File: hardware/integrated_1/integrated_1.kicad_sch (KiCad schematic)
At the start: 6 parts, among them J1 USB4105-GF-A-120, J2 HDMI_A_1.4, J3 DEBUG

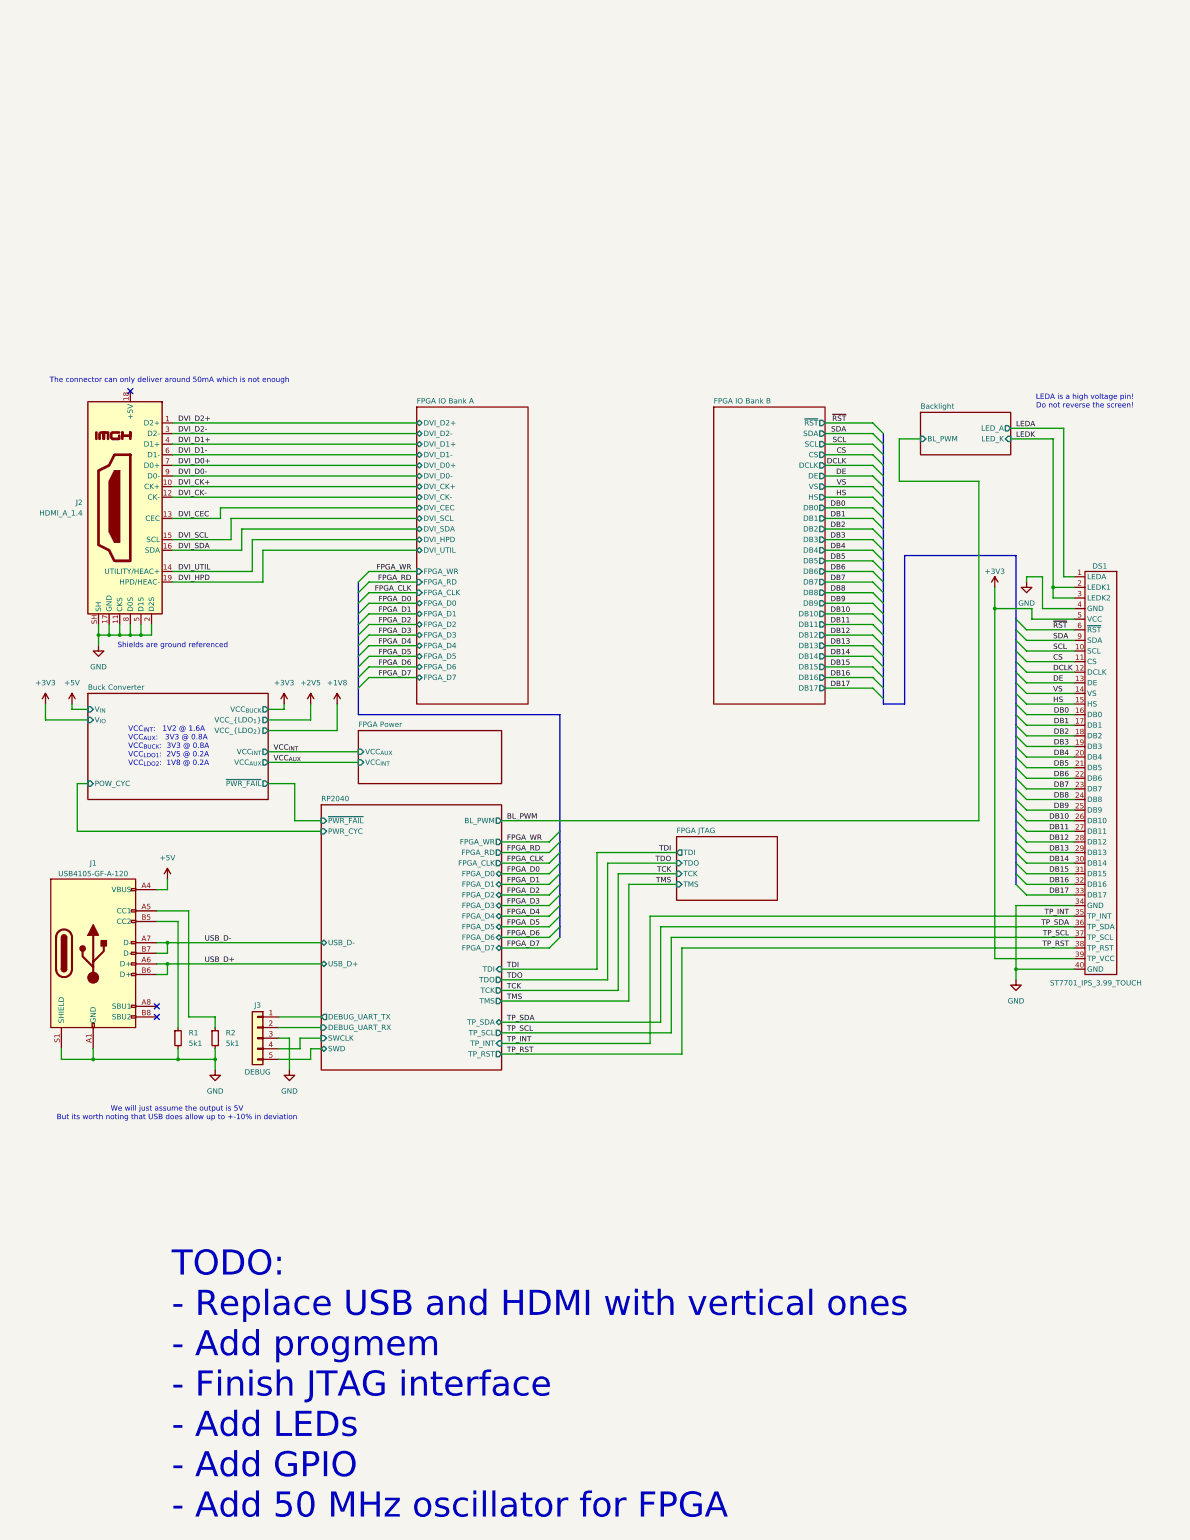
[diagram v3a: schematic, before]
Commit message: reannotated schematic
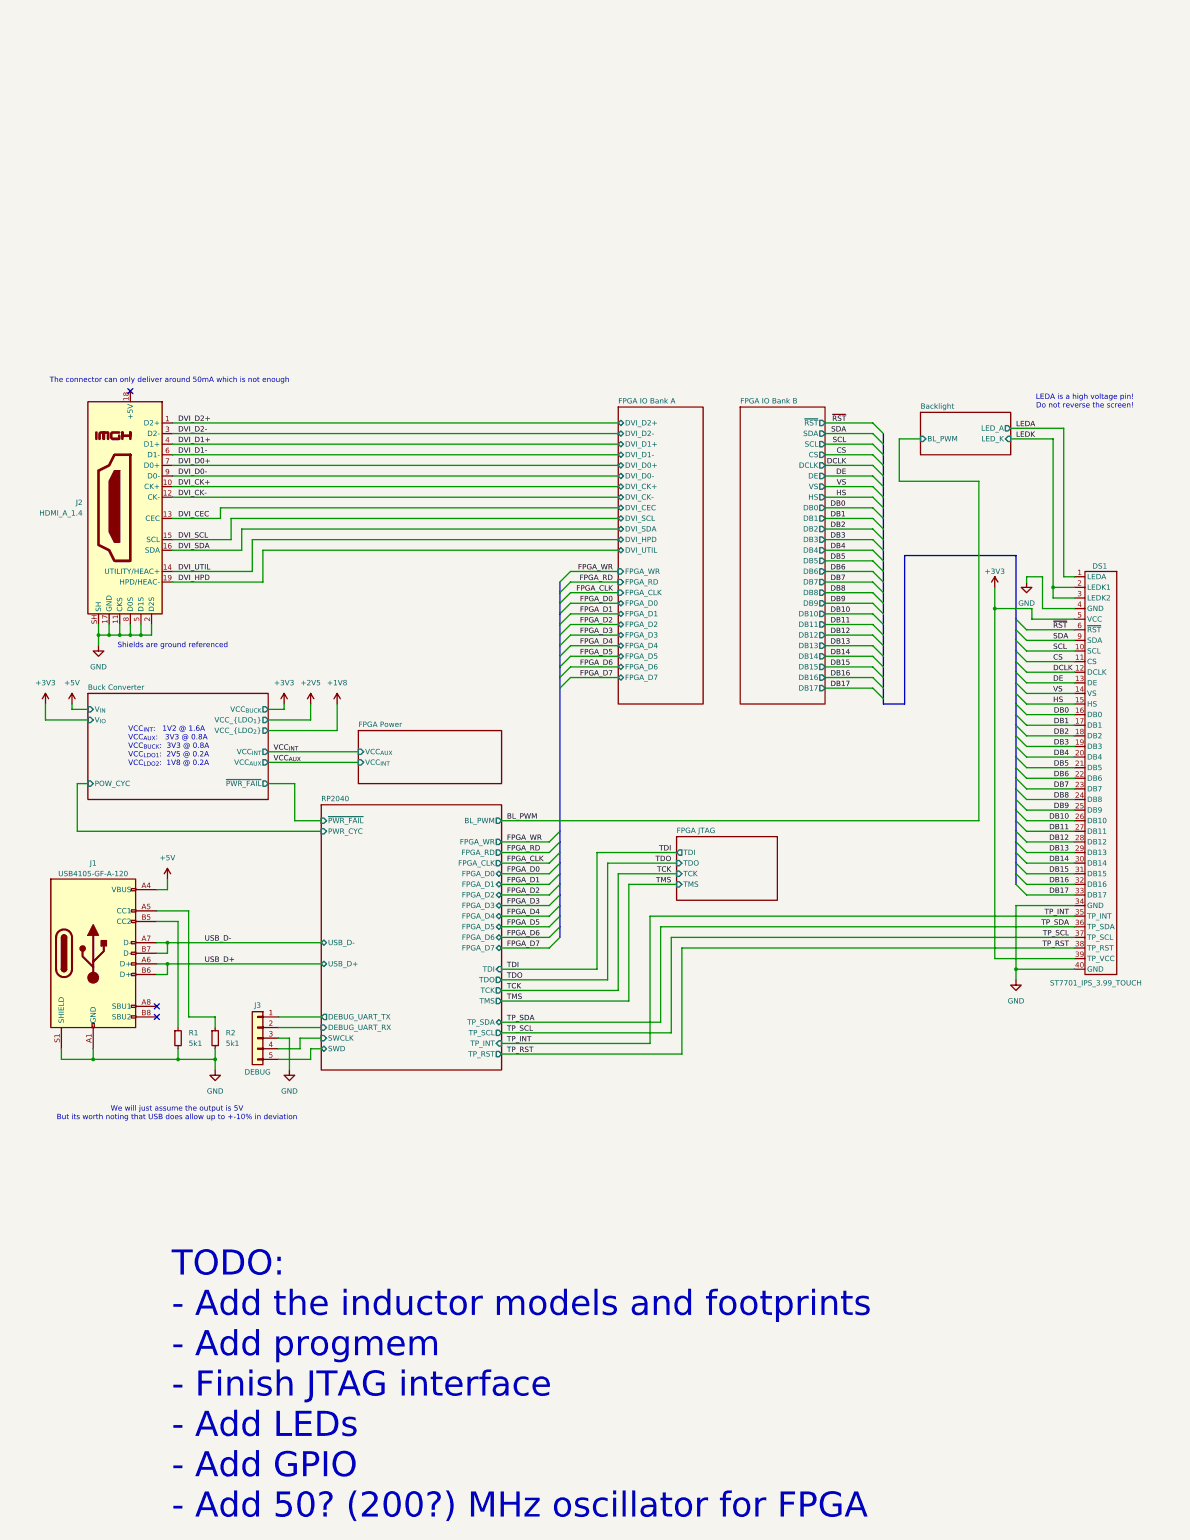
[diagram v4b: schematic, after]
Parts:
- J1: footprint Connector_USB:USB_C_Receptacle_GCT_USB4105-xx-A_16P_TopMnt_Horizontal -> KiCAD Library:CONN_217182-0001_MOL
- J2: footprint Connector_HDMI:HDMI_A_Molex_208658-1001_Horizontal -> KiCAD Library:MOLEX_476591102
- R1, R2: footprint Resistor_SMD:R_0402_1005Metric -> KiCAD Library:R_0402_1005Metric
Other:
- note added: "TODO: - Add the inductor models and footprints - Add progmem - Finish JTAG interface - Add LEDs - Add GPIO - Add 50? (200?) MHz oscillator for FPGA"
- note removed: "TODO: - Replace USB and HDMI with vertical ones - Add progmem - Finish JTAG interface - Add LEDs - Add GPIO - Add 50 MHz oscillator for FPGA"

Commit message: improved top level visually
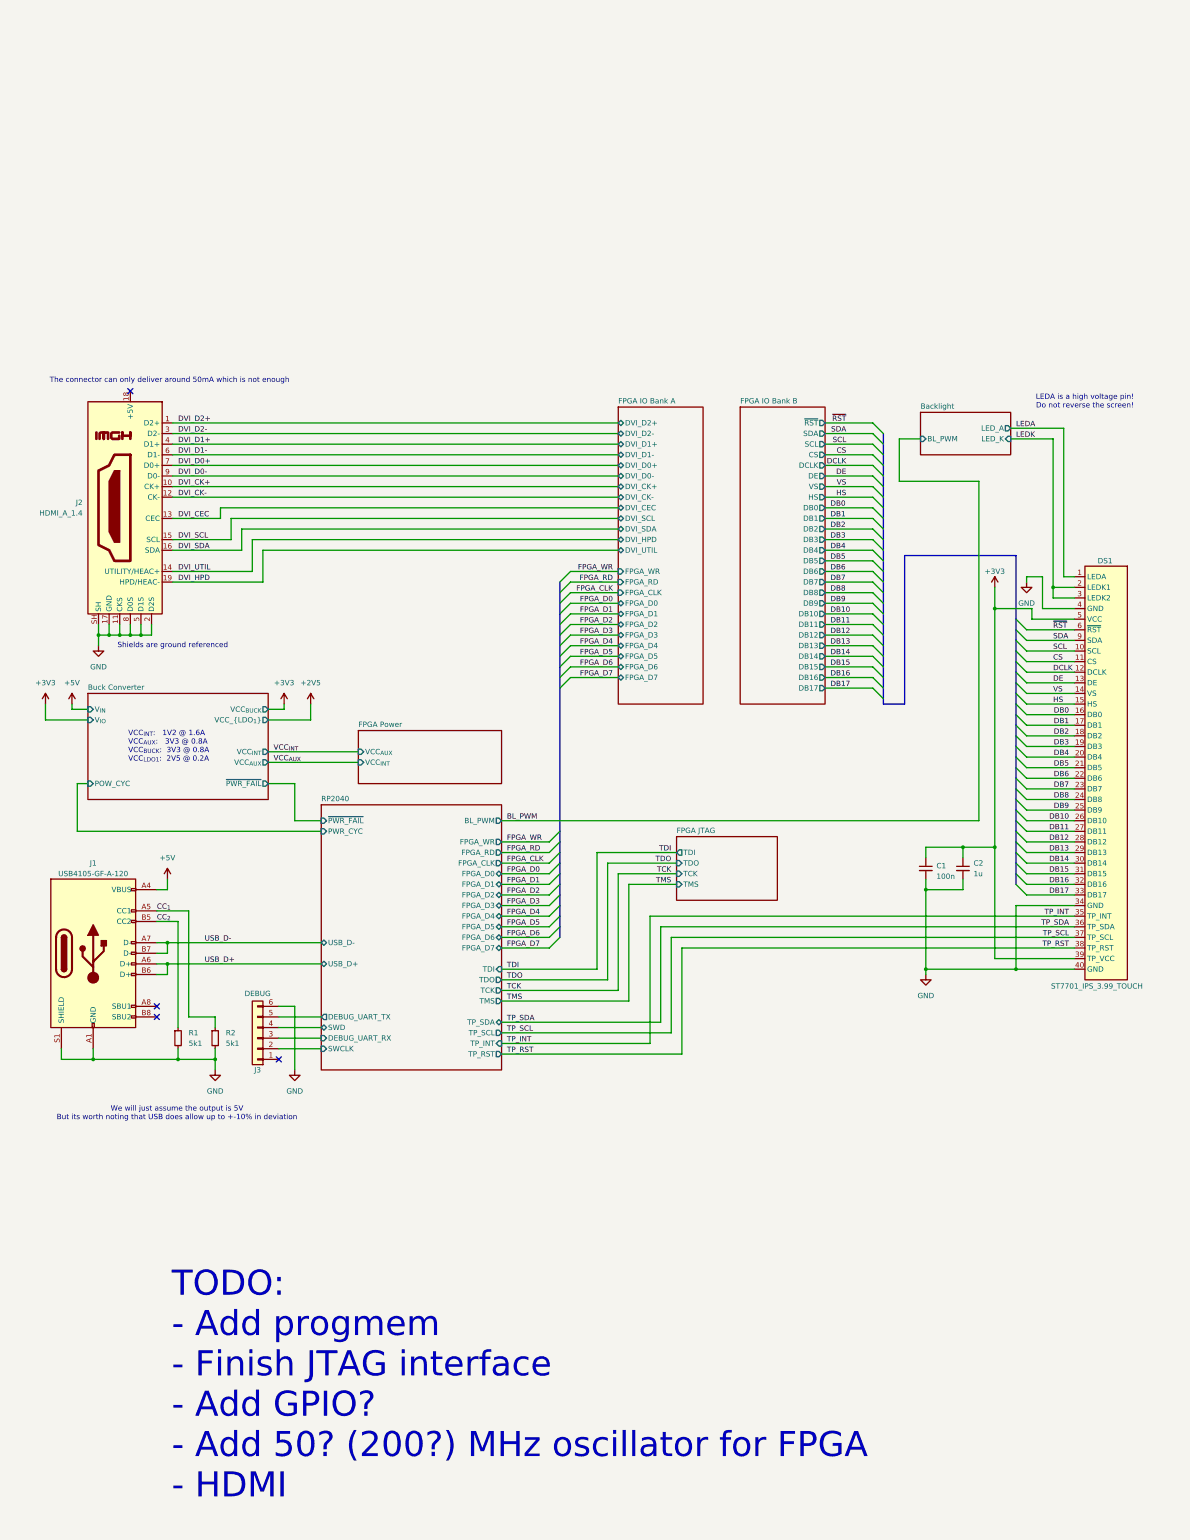
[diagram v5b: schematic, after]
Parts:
- removed J3: DEBUG, symbol Connector_Generic:Conn_01x05
- added C1: 100n, KiCAD Library:C_0402_1005Metric, symbol Device:C_Small
- added C2: 1u, KiCAD Library:C_0402_1005Metric, symbol Device:C_Small
- added J3: DEBUG, Paw-Connect:Paw-Connect_RevB_TC2030-IDC-NL_2x03_P1.27mm_Vertical, symbol Connector_Generic:Conn_01x06
- DS1: footprint KiCAD Library:AMPHENOL_F32Q-1A7H1-11040 -> KiCAD Library:GCT_FFC2B35-40-G_REVA2
- J2: symbol Connector:HDMI_A_1.4 -> Cuprum:HDMI_A_1.4
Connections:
- net +3V3: now also C1.1, C2.1
- net GND: now also DS1.S1 (GND), DS1.S2 (GND), J2.SH1 (SH), J2.SH2 (SH), J2.SH3 (SH), C1.2, C2.2, J3.6 (Pin_6)
- net RP2040/DEBUG_UART_RX: now also J3.3 (Pin_3)
- net RP2040/DEBUG_UART_TX: now also J3.5 (Pin_5)
- net RP2040/SWCLK: now also J3.2 (Pin_2)
- net RP2040/SWD: now also J3.4 (Pin_4)
- net CC_{2}: now reaches J1.B5 (CC2), R1.1
- net CC_{1}: now reaches J1.A5 (CC1), R2.1
- no-connect marks 3 -> 4
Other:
- sheet Buck Converter ports: added none; removed VCC_{LDO_{2}}
- note added: "TODO: - Add progmem - Finish JTAG interface - Add GPIO? - Add 50? (200?) MHz oscillator for FPGA - HDMI"
- note added: "VCC_{INT}: 1V2 @ 1.6A VCC_{AUX}: 3V3 @ 0.8A VCC_{BUCK}: 3V3 @ 0.8A VCC_{LDO1}: 2V5 @ 0.2A"
- note removed: "TODO: - Add the inductor models and footprints - Add progmem - Finish JTAG interface - Add LEDs - Add GPIO - Add 50? (200?) MHz oscillator for FPGA"
- note removed: "VCC_{INT}: 1V2 @ 1.6A VCC_{AUX}: 3V3 @ 0.8A VCC_{BUCK}: 3V3 @ 0.8A VCC_{LDO1}: 2V5 @ 0.2A VCC_{LDO2}: 1V8 @ 0.2A"

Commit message: finalizing the schematic and layout
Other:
- sheet FPGA JTAG ports: added DONE; removed none
- sheet RP2040 ports: added DONE; removed none
- note added: "TODO: - Finish JTAG interface"
- note removed: "TODO: - Add progmem - Finish JTAG interface - Add GPIO? - Add 50? (200?) MHz oscillator for FPGA - HDMI"
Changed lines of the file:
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@@
 	(wire
 		(pts
-			(xy 166.37 148.59) (xy 166.37 171.45)
+			(xy 167.64 148.59) (xy 167.64 173.99)
 		)
 		(stroke
@@
 	(wire
 		(pts
-			(xy 168.91 151.13) (xy 262.89 151.13)
+			(xy 170.18 151.13) (xy 262.89 151.13)
 		)
 		(stroke
@@
 	(wire
 		(pts
-			(xy 125.73 173.99) (xy 161.29 173.99)
+			(xy 125.73 176.53) (xy 162.56 176.53)
 		)
 		(stroke
@@
 	(wire
 		(pts
+			(xy 158.75 166.37) (xy 158.75 138.43)
+		)
+		(stroke
+			(width 0)
+			(type default)
+		)
+	)
+	(wire
+		(pts
 			(xy 243.84 153.67) (xy 262.89 153.67)
 		)
@@
 	(wire
 		(pts
+			(xy 125.73 166.37) (xy 158.75 166.37)
+		)
+		(stroke
+			(width 0)
+			(type default)
+		)
+	)
+	(wire
+		(pts
 			(xy 251.46 74.93) (xy 262.89 74.93)
 		)
@@
 	(wire
 		(pts
+			(xy 158.75 138.43) (xy 167.64 138.43)
+		)
+		(stroke
+			(width 0)
+			(type default)
+		)
+	)
+	(wire
+		(pts
 			(xy 257.81 67.31) (xy 257.81 64.77)
 		)
@@
 	(wire
 		(pts
-			(xy 161.29 143.51) (xy 262.89 143.51)
+			(xy 162.56 143.51) (xy 262.89 143.51)
 		)
 		(stroke
@@
 	(wire
 		(pts
-			(xy 166.37 148.59) (xy 262.89 148.59)
+			(xy 167.64 148.59) (xy 262.89 148.59)
 		)
 		(stroke
@@
 	(wire
 		(pts
-			(xy 161.29 173.99) (xy 161.29 143.51)
+			(xy 162.56 176.53) (xy 162.56 143.51)
 		)
 		(stroke
@@
 	(wire
 		(pts
-			(xy 125.73 176.53) (xy 168.91 176.53)
+			(xy 125.73 179.07) (xy 170.18 179.07)
 		)
 		(stroke
@@
 	(wire
 		(pts
-			(xy 163.83 146.05) (xy 262.89 146.05)
+			(xy 165.1 146.05) (xy 262.89 146.05)
 		)
 		(stroke
@@
 	(wire
 		(pts
-			(xy 163.83 168.91) (xy 125.73 168.91)
+			(xy 165.1 171.45) (xy 125.73 171.45)
 		)
 		(stroke
@@
 	(wire
 		(pts
-			(xy 168.91 176.53) (xy 168.91 151.13)
+			(xy 170.18 179.07) (xy 170.18 151.13)
 		)
 		(stroke
@@
 	(wire
 		(pts
-			(xy 163.83 146.05) (xy 163.83 168.91)
+			(xy 165.1 146.05) (xy 165.1 171.45)
 		)
 		(stroke
@@
 	(wire
 		(pts
-			(xy 166.37 171.45) (xy 125.73 171.45)
+			(xy 167.64 173.99) (xy 125.73 173.99)
 		)
 		(stroke
@@
 		)
 	)
-	(text "TODO:\n- Add progmem\n- Finish JTAG interface\n- Add GPIO?\n- Add 50? (200?) MHz oscillator for FPGA\n- HDMI"
+	(text "TODO:\n- Finish JTAG interface\n"
 		(exclude_from_sim no)
 		(at 46.736 255.778 0)
@@
 		)
 	)
+	(label "DONE"
+		(at 127 166.37 0)
+		(fields_autoplaced yes)
+		(effects
+			(font
+				(size 1.27 1.27)
+			)
+			(justify left bottom)
+		)
+	)
 	(label "FPGA_RD"
 		(at 127 128.27 0)
@@
 	)
 	(label "TP_SCL"
-		(at 127 171.45 0)
+		(at 127.006 173.99 0)
 		(fields_autoplaced yes)
 		(effects
@@
 	)
 	(label "TP_RST"
-		(at 127 176.53 0)
+		(at 127.0085 179.07 0)
 		(fields_autoplaced yes)
 		(effects
@@
 	)
 	(label "TP_INT"
-		(at 127 173.99 0)
+		(at 127 176.53 0)
 		(fields_autoplaced yes)
 		(effects
@@
 	)
 	(label "TP_SDA"
-		(at 127 168.91 0)
+		(at 127.0032 171.45 0)
 		(fields_autoplaced yes)
 		(effects
@@
 	(sheet
 		(at 82.55 116.84)
-		(size 43.18 63.5)
+		(size 43.18 66.04)
 		(fields_autoplaced yes)
 		(stroke
@@
 		)
 		(property "Sheetfile" "sheets/rp2040.kicad_sch"
-			(at 82.55 180.9246 0)
+			(at 82.55 183.4646 0)
 			(effects
 				(font
@@
 		)
 		(pin "TP_RST" output
-			(at 125.73 176.53 0)
+			(at 125.73 179.07 0)
 			(effects
 				(font
@@
 		)
 		(pin "TP_SCL" output
-			(at 125.73 171.45 0)
+			(at 125.73 173.99 0)
 			(effects
 				(font
@@
 		)
 		(pin "TP_INT" input
-			(at 125.73 173.99 0)
+			(at 125.73 176.53 0)
 			(effects
 				(font
@@
 		)
 		(pin "TP_SDA" bidirectional
-			(at 125.73 168.91 0)
+			(at 125.73 171.45 0)
 			(effects
 				(font
@@
 			)
 		)
+		(pin "DONE" input
+			(at 125.73 166.37 0)
+			(effects
+				(font
+					(size 1.27 1.27)
+				)
+				(justify right)
+			)
+		)
 		(instances
 			(project "integrated_1"
@@
 	(sheet
 		(at 167.64 124.46)
-		(size 24.13 15.24)
+		(size 24.13 17.78)
 		(fields_autoplaced yes)
 		(stroke
@@
 		)
 		(property "Sheetfile" "sheets/fpga_jtag.kicad_sch"
-			(at 167.64 140.2846 0)
+			(at 167.64 142.8246 0)
 			(effects
 				(font
@@
 			(effects
 				(font
+					(size 1.27 1.27)
+				)
+				(justify left)
+			)
+		)
+		(pin "DONE" output
+			(at 167.64 138.43 180)
+			(effects
+				(font

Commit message: exported 3d models + added date stamp
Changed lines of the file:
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@@
 	(wire
 		(pts
-			(xy 167.64 148.59) (xy 167.64 173.99)
+			(xy 168.91 148.59) (xy 168.91 173.99)
 		)
 		(stroke
@@
 	(wire
 		(pts
-			(xy 170.18 151.13) (xy 262.89 151.13)
+			(xy 171.45 151.13) (xy 262.89 151.13)
 		)
 		(stroke
@@
 	(wire
 		(pts
-			(xy 125.73 176.53) (xy 162.56 176.53)
+			(xy 125.73 176.53) (xy 163.83 176.53)
 		)
 		(stroke
@@
 	(wire
 		(pts
-			(xy 162.56 143.51) (xy 262.89 143.51)
-		)
-		(stroke
-			(width 0)
-			(type default)
-		)
-	)
-	(wire
-		(pts
-			(xy 167.64 148.59) (xy 262.89 148.59)
+			(xy 163.83 143.51) (xy 262.89 143.51)
+		)
+		(stroke
+			(width 0)
+			(type default)
+		)
+	)
+	(wire
+		(pts
+			(xy 168.91 148.59) (xy 262.89 148.59)
 		)
 		(stroke
@@
 	(wire
 		(pts
-			(xy 162.56 176.53) (xy 162.56 143.51)
+			(xy 163.83 176.53) (xy 163.83 143.51)
 		)
 		(stroke
@@
 	(wire
 		(pts
-			(xy 125.73 179.07) (xy 170.18 179.07)
+			(xy 125.73 179.07) (xy 171.45 179.07)
 		)
 		(stroke
@@
 	(wire
 		(pts
-			(xy 165.1 146.05) (xy 262.89 146.05)
+			(xy 166.37 146.05) (xy 262.89 146.05)
 		)
 		(stroke
@@
 	(wire
 		(pts
-			(xy 165.1 171.45) (xy 125.73 171.45)
+			(xy 166.37 171.45) (xy 125.73 171.45)
 		)
 		(stroke
@@
 	(wire
 		(pts
-			(xy 170.18 179.07) (xy 170.18 151.13)
+			(xy 171.45 179.07) (xy 171.45 151.13)
 		)
 		(stroke
@@
 	(wire
 		(pts
-			(xy 165.1 146.05) (xy 165.1 171.45)
+			(xy 166.37 146.05) (xy 166.37 171.45)
 		)
 		(stroke
@@
 	(wire
 		(pts
-			(xy 167.64 173.99) (xy 125.73 173.99)
-		)
-		(stroke
+			(xy 168.91 173.99) (xy 125.73 173.99)
+		)
+		(stroke

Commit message: fixed critical issue - display connector was mirrored
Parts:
- DS1: footprint KiCAD Library:GCT_FFC2B35-40-G_REVA2 -> KiCAD Library:GCT_FFC2B35-40-G_REVA2_INV
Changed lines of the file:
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@@
 			)
 		)
-		(property "Footprint" "KiCAD Library:GCT_FFC2B35-40-G_REVA2"
+		(property "Footprint" "KiCAD Library:GCT_FFC2B35-40-G_REVA2_INV"
 			(at 262.89 74.93 0)
 			(effects
